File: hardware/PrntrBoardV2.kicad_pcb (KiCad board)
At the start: 2 copper layers, 148.7 x 104.3 mm, 253 parts, among them J1 Fan, J10 Conn_01x03_Male, J11 Conn_01x03_Male, J12 Conn_01x03_Male, J13 Conn_01x03_Male, J14 Conn_01x03_Male, J15 Conn_01x03_Male, J16 JST XH, J17 KF350, J18 JST XH, J19 JST XH, J2 Fan, J20 KF350, J21 JST XH, J22 Fan, J23 Fan, J3 USB_B_Micro, J4 JST XH, J5 KF129, J6 KF350, J7 Conn_01x03_Male, J8 Conn_01x03_Male, J9 Conn_01x03_Male, U1 74LVC125, U2 STM32F407VETx, U3 24LC64, U4 AMS1117-3.3, U5 DCBuck, U6 74HCT02, Y1 8MHz

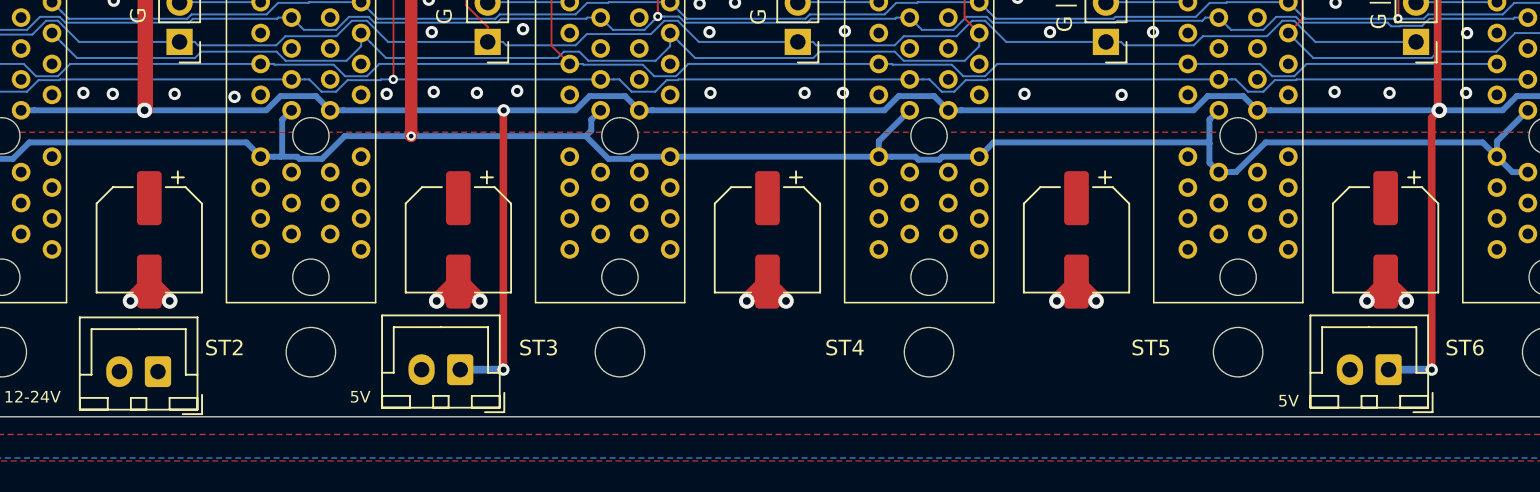
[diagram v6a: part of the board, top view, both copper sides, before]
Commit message: Fix 5V fan location.
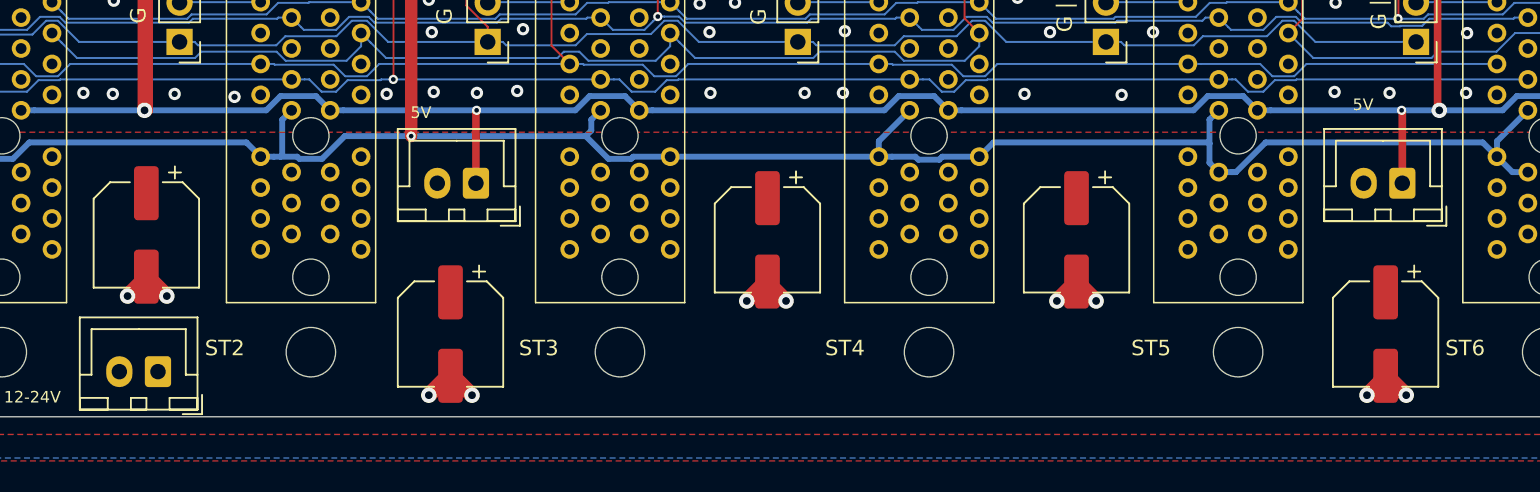
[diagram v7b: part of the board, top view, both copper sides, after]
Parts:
- moved J1 12.1 mm to (72.1, 148.3)
- moved J2 12.1 mm to (132.1, 148.3)
- moved C49 6.12 mm to (70.5, 158.1)
- moved C52 6.10 mm to (131.0, 158.1)
- moved C48 0.37 mm to (50.8, 151.7)
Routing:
- net 5V: track 513.0 -> 483.1 mm, vias 17 -> 16
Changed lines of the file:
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@@
     (thickness 1.6)
     (drawings 152)
-    (tracks 4099)
+    (tracks 4097)
     (modules 253)
     (nets 177)
@@
   )
   (module "Connector_JST:JST_XH_B2B-XH-A_1x02_P2.50mm_Vertical" (layer "F.Cu")
-    (at 131.191 160.401 180)
+    (at 132.08 148.336 180)
     (descr "JST XH series connector, B2B-XH-A (http://www.jst-mfg.com/product/pdf/eng/eXH.pdf), generated with kicad-footprint-generator")
     (tags "connector JST XH vertical")
@@
   )
   (module "Connector_JST:JST_XH_B2B-XH-A_1x02_P2.50mm_Vertical" (layer "F.Cu")
-    (at 71.12 160.401 180)
+    (at 72.136 148.336 180)
     (descr "JST XH series connector, B2B-XH-A (http://www.jst-mfg.com/product/pdf/eng/eXH.pdf), generated with kicad-footprint-generator")
     (tags "connector JST XH vertical")
@@
   )
   (module "Capacitor_SMD:CP_Elec_6.3x7.7" (layer "F.Cu")
-    (at 131 152 270)
+    (at 131 158.096 270)
     (descr "SMD capacitor, aluminum electrolytic, Nichicon, 6.3x7.7mm")
     (tags "capacitor electrolytic")
@@
   )
   (module "Capacitor_SMD:CP_Elec_6.3x7.7" (layer "F.Cu")
-    (at 71 152 270)
+    (at 70.492 158.096 270)
     (descr "SMD capacitor, aluminum electrolytic, Nichicon, 6.3x7.7mm")
     (tags "capacitor electrolytic")
@@
   )
   (module "Capacitor_SMD:CP_Elec_6.3x7.7" (layer "F.Cu")
-    (at 51 152 270)
+    (at 50.8095 151.6825 270)
     (descr "SMD capacitor, aluminum electrolytic, Nichicon, 6.3x7.7mm")
     (tags "capacitor electrolytic")
@@
     (effects (font (size 1 1) (thickness 0.15)) (justify mirror))
   )
-  (gr_text "5V\n+  -" (at 130.048 157.861) (layer "B.SilkS")
+  (gr_text "5V\n+  -" (at 130.81 145.542) (layer "B.SilkS")
     (effects (font (size 1 1) (thickness 0.15)) (justify mirror))
   )
-  (gr_text "5V\n+  -" (at 69.977 157.861) (layer "B.SilkS")
+  (gr_text "5V\n+  -" (at 70.866 145.542) (layer "B.SilkS")
     (effects (font (size 1 1) (thickness 0.15)) (justify mirror))
   )
@@
     (effects (font (size 1 1) (thickness 0.15)))
   )
-  (gr_text "5V" (at 64.643 162.179) (layer "F.SilkS")
+  (gr_text "5V" (at 68.58 143.764) (layer "F.SilkS")
     (effects (font (size 0.75 0.75) (thickness 0.12)))
   )
-  (gr_text "5V" (at 124.714 162.433) (layer "F.SilkS")
+  (gr_text "5V" (at 129.54 143.256) (layer "F.SilkS")
     (effects (font (size 0.75 0.75) (thickness 0.12)))
   )
@@
   (via (at 109.093 101.727) (size 0.6) (drill 0.3) (layers "F.Cu" "B.Cu") (net 83))
   (via (at 108.585 101.092) (size 0.6) (drill 0.3) (layers "F.Cu" "B.Cu") (net 84))
-  (via (at 129.794 155.956) (size 1) (drill 0.5) (layers "F.Cu" "B.Cu") (net 2))
-  (segment (start 131 154.7) (end 131 154.75) (width 1) (layer "F.Cu") (net 2))
-  (segment (start 131 154.75) (end 129.794 155.956) (width 1) (layer "F.Cu") (net 2))
-  (via (at 132.334 155.956) (size 1) (drill 0.5) (layers "F.Cu" "B.Cu") (net 2))
-  (segment (start 131 154.7) (end 131.078 154.7) (width 1) (layer "F.Cu") (net 2))
-  (segment (start 131.078 154.7) (end 132.334 155.956) (width 1) (layer "F.Cu") (net 2))
+  (via (at 129.794 162.052) (size 1) (drill 0.5) (layers "F.Cu" "B.Cu") (net 2))
+  (segment (start 131 160.796) (end 131 160.846) (width 1) (layer "F.Cu") (net 2))
+  (segment (start 131 160.846) (end 129.794 162.052) (width 1) (layer "F.Cu") (net 2))
+  (via (at 132.334 162.052) (size 1) (drill 0.5) (layers "F.Cu" "B.Cu") (net 2))
+  (segment (start 131 160.796) (end 131.078 160.796) (width 1) (layer "F.Cu") (net 2))
+  (segment (start 131.078 160.796) (end 132.334 162.052) (width 1) (layer "F.Cu") (net 2))
   (via (at 109.728 155.956) (size 1) (drill 0.5) (layers "F.Cu" "B.Cu") (net 2))
   (segment (start 111 154.7) (end 110.984 154.7) (width 1) (layer "F.Cu") (net 2))
@@
   (via (at 92.202 155.956) (size 1) (drill 0.5) (layers "F.Cu" "B.Cu") (net 2))
   (segment (start 91 154.754) (end 92.202 155.956) (width 1) (layer "F.Cu") (net 2))
-  (via (at 69.596 155.956) (size 1) (drill 0.5) (layers "F.Cu" "B.Cu") (net 2))
-  (segment (start 71 154.7) (end 70.852 154.7) (width 1) (layer "F.Cu") (net 2))
-  (segment (start 70.852 154.7) (end 69.596 155.956) (width 1) (layer "F.Cu") (net 2))
-  (via (at 72.39 155.956) (size 1) (drill 0.5) (layers "F.Cu" "B.Cu") (net 2))
-  (segment (start 71 154.7) (end 71.134 154.7) (width 1) (layer "F.Cu") (net 2))
-  (segment (start 71.134 154.7) (end 72.39 155.956) (width 1) (layer "F.Cu") (net 2))
-  (via (at 49.784 155.956) (size 1) (drill 0.5) (layers "F.Cu" "B.Cu") (net 2))
-  (segment (start 51 154.7) (end 51 154.74) (width 1) (layer "F.Cu") (net 2))
-  (segment (start 51 154.74) (end 49.784 155.956) (width 1) (layer "F.Cu") (net 2))
-  (via (at 52.324 155.956) (size 1) (drill 0.5) (layers "F.Cu" "B.Cu") (net 2))
-  (segment (start 51 154.7) (end 51.068 154.7) (width 1) (layer "F.Cu") (net 2))
-  (segment (start 51.068 154.7) (end 52.324 155.956) (width 1) (layer "F.Cu") (net 2))
+  (via (at 69.088 162.052) (size 1) (drill 0.5) (layers "F.Cu" "B.Cu") (net 2))
+  (segment (start 70.492 160.796) (end 70.344 160.796) (width 1) (layer "F.Cu") (net 2))
+  (segment (start 70.344 160.796) (end 69.088 162.052) (width 1) (layer "F.Cu") (net 2))
+  (via (at 71.882 162.052) (size 1) (drill 0.5) (layers "F.Cu" "B.Cu") (net 2))
+  (segment (start 70.492 160.796) (end 70.626 160.796) (width 1) (layer "F.Cu") (net 2))
+  (segment (start 70.626 160.796) (end 71.882 162.052) (width 1) (layer "F.Cu") (net 2))
+  (via (at 49.5935 155.6385) (size 1) (drill 0.5) (layers "F.Cu" "B.Cu") (net 2))
+  (segment (start 50.8095 154.3825) (end 50.8095 154.4225) (width 1) (layer "F.Cu") (net 2))
+  (segment (start 50.8095 154.4225) (end 49.5935 155.6385) (width 1) (layer "F.Cu") (net 2))
+  (via (at 52.1335 155.6385) (size 1) (drill 0.5) (layers "F.Cu" "B.Cu") (net 2))
+  (segment (start 50.8095 154.3825) (end 50.8775 154.3825) (width 1) (layer "F.Cu") (net 2))
+  (segment (start 50.8775 154.3825) (end 52.1335 155.6385) (width 1) (layer "F.Cu") (net 2))
   (via (at 29.718 155.956) (size 1) (drill 0.5) (layers "F.Cu" "B.Cu") (net 2))
   (segment (start 31 154.7) (end 30.974 154.7) (width 1) (layer "F.Cu") (net 2))
@@
   (segment (start 102.706 143.618) (end 101.784499 142.696499) (width 0.381) (layer "B.Cu") (net 10))
   (segment (start 63.560184 143.618) (end 62.706 143.618) (width 0.381) (layer "B.Cu") (net 10))
-  (segment (start 78.569822 143.618) (end 63.560184 143.618) (width 0.381) (layer "B.Cu") (net 10))
   (segment (start 79.491323 142.696499) (end 78.569822 143.618) (width 0.381) (layer "B.Cu") (net 10))
   (segment (start 81.784499 142.696499) (end 79.491323 142.696499) (width 0.381) (layer "B.Cu") (net 10))
@@
   (segment (start 103.597012 77.292287) (end 103.597012 89.563783) (width 0.127) (layer "F.Cu") (net 165))
   (segment (start 102.937077 76.632352) (end 103.597012 77.292287) (width 0.127) (layer "F.Cu") (net 165))
-  (via (at 73.914 160.401) (size 0.8) (drill 0.4) (layers "F.Cu" "B.Cu") (net 10))
-  (segment (start 71.12 160.401) (end 73.914 160.401) (width 0.5) (layer "B.Cu") (net 10))
-  (via (at 73.933 143.618) (size 0.8) (drill 0.4) (layers "F.Cu" "B.Cu") (net 10))
-  (segment (start 73.914 160.401) (end 73.914 143.637) (width 0.5) (layer "F.Cu") (net 10))
-  (segment (start 73.914 143.637) (end 73.933 143.618) (width 0.5) (layer "F.Cu") (net 10))
-  (via (at 133.985 160.401) (size 0.8) (drill 0.4) (layers "F.Cu" "B.Cu") (net 10))
-  (segment (start 131.191 160.401) (end 133.985 160.401) (width 0.5) (layer "B.Cu") (net 10))
-  (segment (start 133.985 144.107) (end 134.474 143.618) (width 0.5) (layer "F.Cu") (net 10))
-  (segment (start 133.985 160.401) (end 133.985 144.107) (width 0.5) (layer "F.Cu") (net 10))
   (via (at 130.429 132.207) (size 0.8) (drill 0.4) (layers "F.Cu" "B.Cu") (net 2))
   (via (at 127.889 132.207) (size 0.8) (drill 0.4) (layers "F.Cu" "B.Cu") (net 2))
+  (via (at 72.1805 143.618) (size 0.6) (drill 0.3) (layers "F.Cu" "B.Cu") (net 10))
+  (segment (start 72.136 143.6625) (end 72.1805 143.618) (width 0.5) (layer "F.Cu") (net 10))
+  (segment (start 72.136 148.336) (end 72.136 143.6625) (width 0.5) (layer "F.Cu") (net 10))
+  (segment (start 78.569822 143.618) (end 72.1805 143.618) (width 0.381) (layer "B.Cu") (net 10))
+  (segment (start 72.1805 143.618) (end 63.560184 143.618) (width 0.381) (layer "B.Cu") (net 10))
+  (via (at 132.0355 143.618) (size 0.6) (drill 0.3) (layers "F.Cu" "B.Cu") (net 10))
+  (segment (start 132.08 148.336) (end 132.08 143.6625) (width 0.5) (layer "F.Cu") (net 10))
+  (segment (start 132.08 143.6625) (end 132.0355 143.618) (width 0.5) (layer "F.Cu") (net 10))
   (zone (net 2) (net_name "GND") (layer "B.Cu") (hatch edge 0.508)
     (connect_pads (clearance 0.1524))
